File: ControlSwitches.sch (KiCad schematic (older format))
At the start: 17 parts, among them J6 Backup, SW1 HAZARD, SW2 CRUISE_SET, SW3 CRUISE, SW4 F/R_SW, SW5 HEADLIGHT_SW, SW6 BACKUP_SW, SW7 TURN_SIGNAL_SW, SW8 REGEN_SW

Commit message: Finished current updates to the board
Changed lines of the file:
@@
 Wire Wire Line
 	7950 4700 8800 4700
+Text Label 8800 4900 2    50   ~ 0
+FOR_SW
+Text Label 8800 4700 2    50   ~ 0
+REV_SW
 $EndSCHEMATC

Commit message: Changed switches
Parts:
- added R?: 10k, symbol Device:R_US
- SW1, SW5, SW6: footprint Connector_Molex:Molex_Micro-Fit_3.0_43650-0300_1x03_P3.00mm_Horizontal -> Connector_Molex:Molex_Micro-Fit_3.0_43650-0200_1x02_P3.00mm_Horizontal; symbol Switch:SW_SPDT -> Switch:SW_SPST
- SW2, SW3, SW8: footprint Connector_Molex:Molex_Micro-Fit_3.0_43650-0300_1x03_P3.00mm_Horizontal -> Connector_Molex:Molex_Micro-Fit_3.0_43650-0200_1x02_P3.00mm_Horizontal; symbol Switch:SW_SPDT -> Switch:SW_Push
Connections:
- net +3V3: no longer R5.2, R6.2, R7.2, R9.2, SW5.3 (C)
- net Backup: now also SW6.1 (A); no longer SW6.2 (B)
- net CRUZ_EN: now also SW3.1; no longer SW3.2 (B)
- net CRUZ_ST: now also SW2.1; no longer SW2.2 (B)
- net GND: now also R5.2, R6.2, R7.2, R9.2, R?.2; no longer SW1.1 (A), SW2.1 (A), SW3.1 (A), SW5.1 (A), SW8.1 (A)
- net GNDPWR: now also SW6.2 (B); no longer SW6.1 (A)
- net HZD_SW: now also SW1.1 (A); no longer SW1.2 (B)
- net Headlight_SW: now also SW5.1 (A); no longer SW5.2 (B)
- net REGEN_SW: now also SW8.1; no longer SW8.2 (B)
- net at R6.1: now also SW2.2; no longer SW2.3 (C)
- net at R7.1: now also SW3.2; no longer SW3.3 (C)
- net at R5.1: now also SW1.2 (B); no longer SW1.3 (C)
- net at R9.1: now also SW8.2; no longer SW8.3 (C)
- removed net +12V: SW6.3 (C)
- new net: R?.1, SW5.2 (B)
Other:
- moved on the sheet: J2, R13, R14, R15, R16, R17, R19, R20, R9, SW4, SW7

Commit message: Board finished with the new changes, needs to be checked
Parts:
- R21: renamed from R?; footprint (none) -> Resistor_SMD:R_0805_2012Metric
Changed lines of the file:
@@
 	3250 3200 3400 3200
 $Comp
-L power:GND #PWR?
+L power:GND #PWR011
 U 1 1 600A77A8
 P 3250 3200
-F 0 "#PWR?" H 3250 2950 50  0001 C CNN
+F 0 "#PWR011" H 3250 2950 50  0001 C CNN
 F 1 "GND" H 3255 3027 50  0000 C CNN
 F 2 "" H 3250 3200 50  0001 C CNN
@@
 $EndComp
 $Comp
-L Device:R_US R?
+L Device:R_US R21
 U 1 1 600A937F
 P 5450 4050
-F 0 "R?" V 5245 4050 50  0000 C CNN
+F 0 "R21" V 5245 4050 50  0000 C CNN
 F 1 "10k" V 5336 4050 50  0000 C CNN
-F 2 "" V 5490 4040 50  0001 C CNN
+F 2 "Resistor_SMD:R_0805_2012Metric" V 5490 4040 50  0001 C CNN
 F 3 "~" H 5450 4050 50  0001 C CNN
 	1    5450 4050

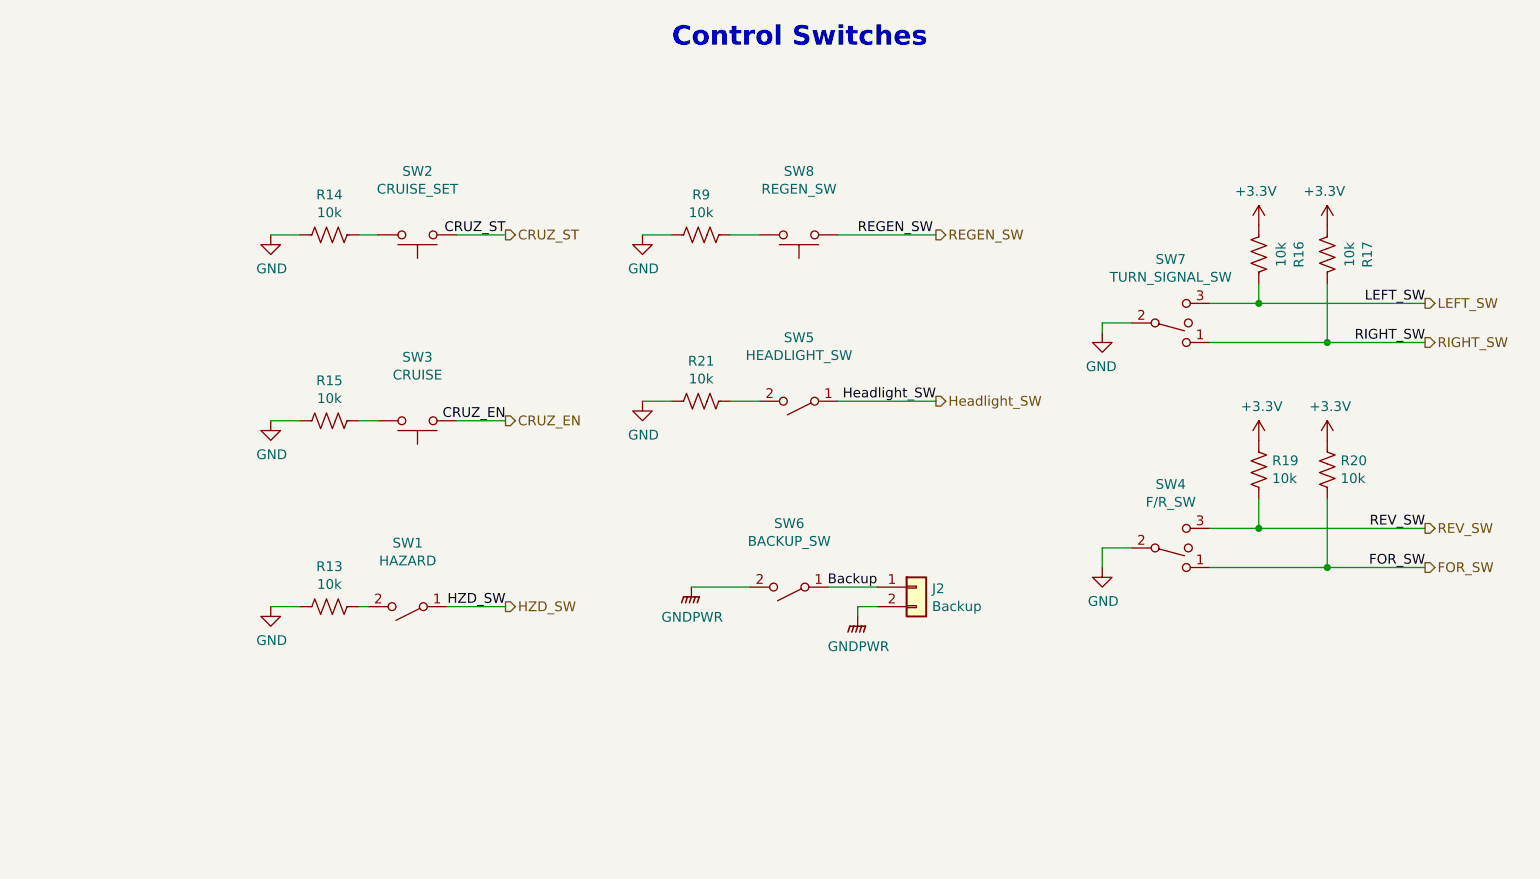
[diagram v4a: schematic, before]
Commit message: Fixes switch/button circuitry
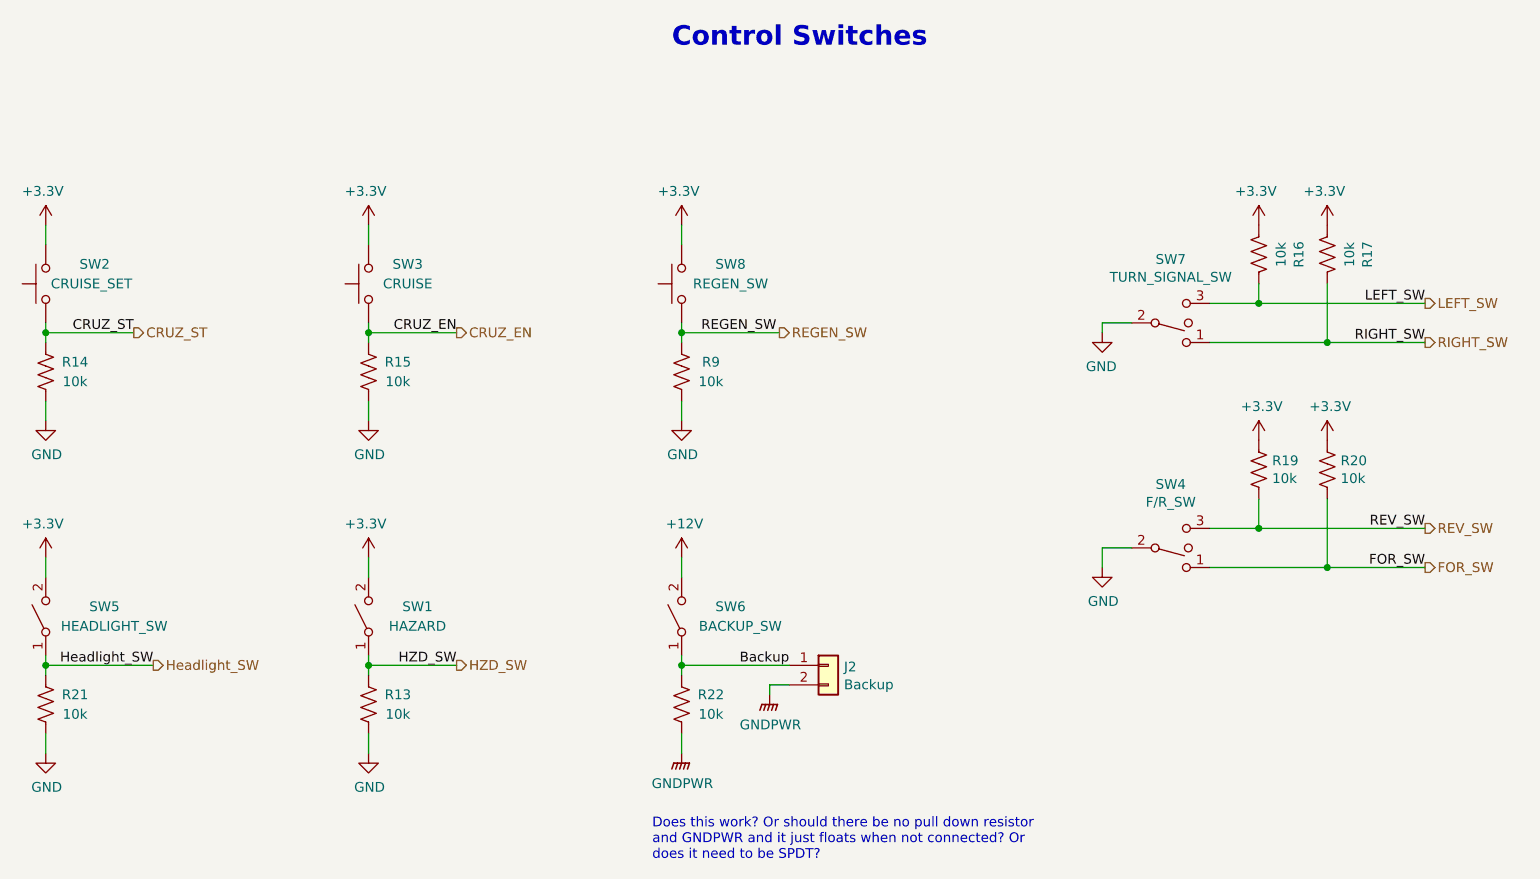
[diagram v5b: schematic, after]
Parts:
- added R22: 10k, Resistor_SMD:R_0805_2012Metric, symbol Device:R_US
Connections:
- net +3V3: now also SW1.2 (B), SW2.2, SW3.2, SW5.2 (B), SW8.2
- net Backup: now also R22.2
- net CRUZ_EN: now also R7.2
- net CRUZ_ST: now also R6.1
- net GND: now also R21.1, R5.1, R7.1, R9.1; no longer R21.2, R5.2, R7.2, R9.2
- net GNDPWR: now also R22.1; no longer SW6.2 (B)
- net HZD_SW: now also R5.2
- net Headlight_SW: now also R21.2
- net REGEN_SW: now also R9.2
- new net +12V: SW6.2 (B)
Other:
- note added: "Does this work? Or should there be no pull down resistor\nand GNDPWR and it just floats when not connected? Or \ndoes it need to be SPDT?"
- moved on the sheet: J2, R13, R14, R15, R21, R9, SW1, SW2, SW3, SW5, SW6, SW8

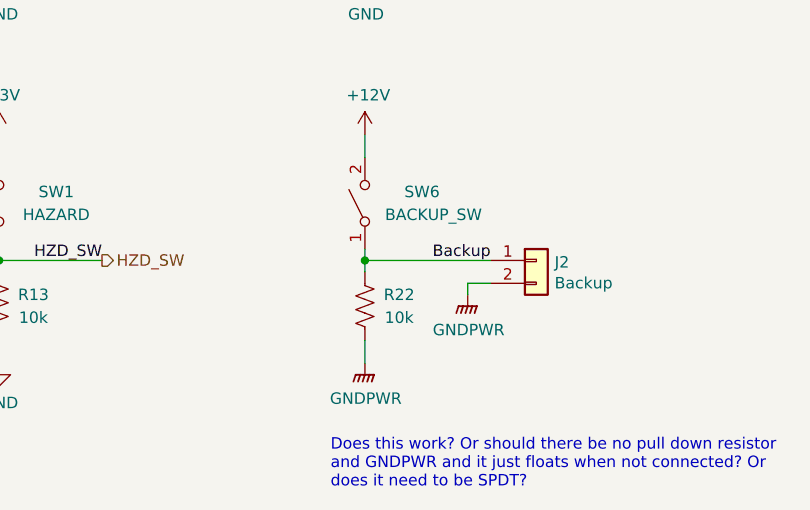
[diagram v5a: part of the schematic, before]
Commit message: isoSPI -> SPI 2
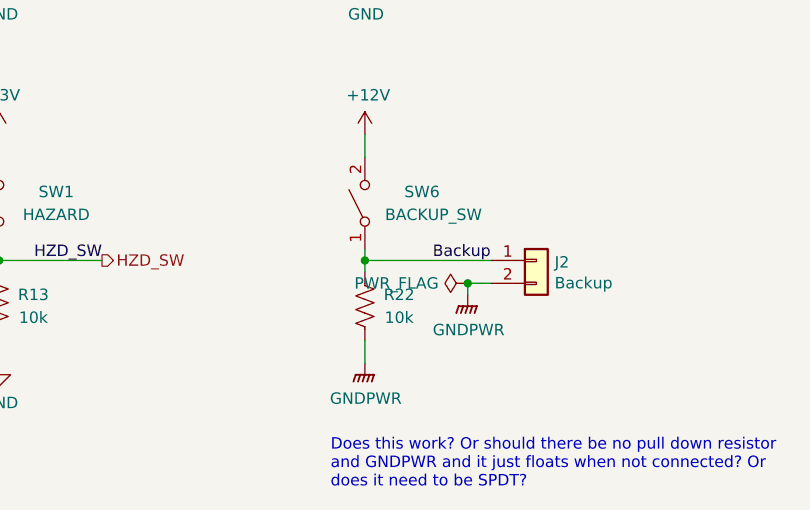
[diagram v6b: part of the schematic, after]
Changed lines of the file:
@@
 Text Notes 5200 6400 0    50   ~ 0
 Does this work? Or should there be no pull down resistor\nand GNDPWR and it just floats when not connected? Or \ndoes it need to be SPDT?
+$Comp
+L power:PWR_FLAG #FLG0102
+U 1 1 61A04CAB
+P 5800 5500
+F 0 "#FLG0102" H 5800 5575 50  0001 C CNN
+F 1 "PWR_FLAG" V 5800 5627 50  0000 L CNN
+F 2 "" H 5800 5500 50  0001 C CNN
+F 3 "~" H 5800 5500 50  0001 C CNN
+	1    5800 5500
+	0    -1   -1   0
+$EndComp
+Connection ~ 5800 5500
 $EndSCHEMATC

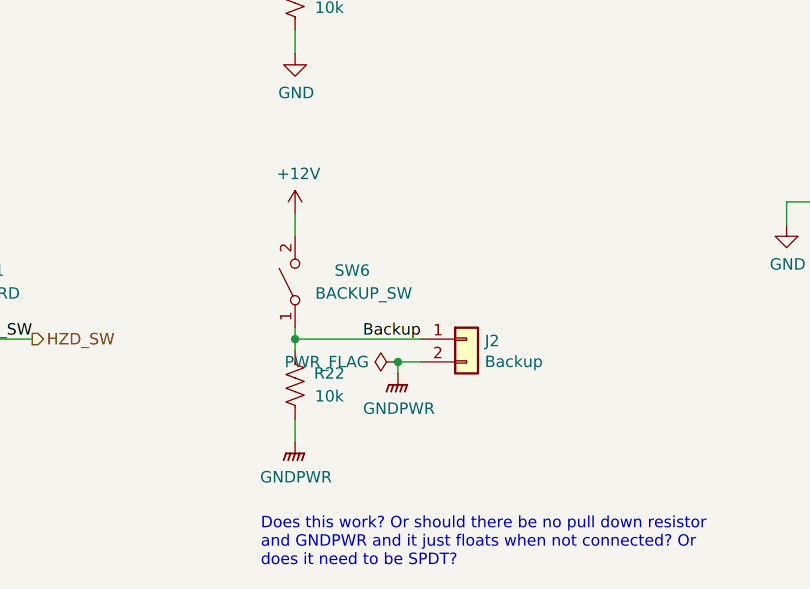
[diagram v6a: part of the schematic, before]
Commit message: Deleted backup camera
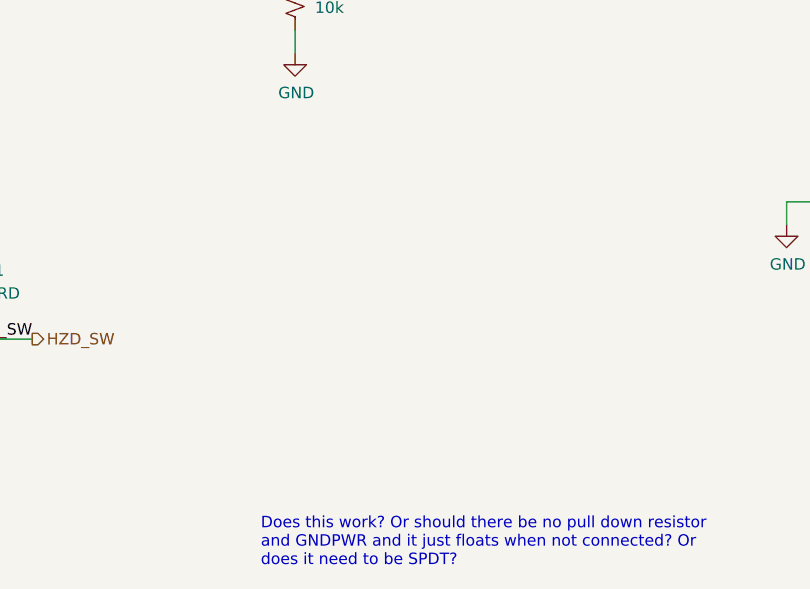
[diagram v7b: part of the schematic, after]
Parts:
- removed J6: Backup, Connector_Molex:Molex_Micro-Fit_3.0_43650-0200_1x02_P3.00mm_Horizontal, symbol Connector_Generic:Conn_01x02
- removed R22: 10k, Resistor_SMD:R_0805_2012Metric, symbol Device:R_US
- removed SW6: BACKUP_SW, Connector_Molex:Molex_Micro-Fit_3.0_43650-0200_1x02_P3.00mm_Horizontal, symbol Switch:SW_SPST
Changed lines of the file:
@@
 RIGHT_SW
-$Comp
-L Switch:SW_SPST SW?
-U 1 1 5F95FD6B
-P 5350 5150
-AR Path="/5F95FD6B" Ref="SW?"  Part="1"
-AR Path="/5F958945/5F95FD6B" Ref="SW6"  Part="1"
-AR Path="/5F78B3EB/5F95FD6B" Ref="SW6"  Part="1"
-F 0 "SW6" V 5400 4900 50  0000 C CNN
-F 1 "BACKUP_SW" V 5300 4850 50  0000 C CNN
-F 2 "Connector_Molex:Molex_Micro-Fit_3.0_43650-0200_1x02_P3.00mm_Horizontal" H 5350 5150 50  0001 C CNN
-F 3 "~" H 5350 5150 50  0001 C CNN
-	1    5350 5150
-	0    -1   -1   0
-$EndComp
-Text Label 5900 5400 2    50   ~ 0
-Backup
 $Comp
 L power:GND #PWR?
@@
 	0    -1   -1   0
 $EndComp
-$Comp
-L Connector_Generic:Conn_01x02 J?
-U 1 1 5F95FD8F
-P 6100 5400
-AR Path="/5F95FD8F" Ref="J?"  Part="1"
-AR Path="/5F958945/5F95FD8F" Ref="J6"  Part="1"
-AR Path="/5F78B3EB/5F95FD8F" Ref="J2"  Part="1"
-F 0 "J2" H 6180 5392 50  0000 L CNN
-F 1 "Backup" H 6180 5301 50  0000 L CNN
-F 2 "Connector_Molex:Molex_Micro-Fit_3.0_43650-0200_1x02_P3.00mm_Horizontal" H 6100 5400 50  0001 C CNN
-F 3 "~" H 6100 5400 50  0001 C CNN
-	1    6100 5400
-	1    0    0    -1
-$EndComp
-$Comp
-L power:GNDPWR #PWR?
-U 1 1 5F95FD95
-P 5800 5550
-AR Path="/5F95FD95" Ref="#PWR?"  Part="1"
-AR Path="/5F958945/5F95FD95" Ref="#PWR0138"  Part="1"
-AR Path="/5F78B3EB/5F95FD95" Ref="#PWR0131"  Part="1"
-F 0 "#PWR0131" H 5800 5350 50  0001 C CNN
-F 1 "GNDPWR" H 5804 5396 50  0000 C CNN
-F 2 "" H 5800 5500 50  0001 C CNN
-F 3 "" H 5800 5500 50  0001 C CNN
-	1    5800 5550
-	1    0    0    -1
-$EndComp
-Wire Wire Line
-	5800 5550 5800 5500
-Wire Wire Line
-	5800 5500 5900 5500
 $Comp
 L Device:R_US R?
@@
 Wire Wire Line
 	3750 5750 3750 5850
-$Comp
-L power:+12V #PWR026
-U 1 1 5FE1F02E
-P 5350 4850
-F 0 "#PWR026" H 5350 4700 50  0001 C CNN
-F 1 "+12V" H 5365 5023 50  0000 C CNN
-F 2 "" H 5350 4850 50  0001 C CNN
-F 3 "" H 5350 4850 50  0001 C CNN
-	1    5350 4850
-	1    0    0    -1
-$EndComp
-$Comp
-L Device:R_US R?
-U 1 1 5FE23776
-P 5350 5600
-AR Path="/5FE23776" Ref="R?"  Part="1"
-AR Path="/5F958945/5FE23776" Ref="R?"  Part="1"
-AR Path="/5F78B3EB/5FE23776" Ref="R22"  Part="1"
-F 0 "R22" H 5200 5550 50  0000 C CNN
-F 1 "10k" H 5200 5650 50  0000 C CNN
-F 2 "Resistor_SMD:R_0805_2012Metric" V 5390 5590 50  0001 C CNN
-F 3 "~" H 5350 5600 50  0001 C CNN
-F 4 "71-CRCW080510K0FKEAC " H 5350 5600 50  0001 C CNN "Mouser Part Number"
-	1    5350 5600
-	-1   0    0    1
-$EndComp
-$Comp
-L power:GNDPWR #PWR?
-U 1 1 5FE24C12
-P 5350 5850
-AR Path="/5FE24C12" Ref="#PWR?"  Part="1"
-AR Path="/5F958945/5FE24C12" Ref="#PWR?"  Part="1"
-AR Path="/5F78B3EB/5FE24C12" Ref="#PWR027"  Part="1"
-F 0 "#PWR027" H 5350 5650 50  0001 C CNN
-F 1 "GNDPWR" H 5354 5696 50  0000 C CNN
-F 2 "" H 5350 5800 50  0001 C CNN
-F 3 "" H 5350 5800 50  0001 C CNN
-	1    5350 5850
-	1    0    0    -1
-$EndComp
-Wire Wire Line
-	5350 4850 5350 4950
-Wire Wire Line
-	5350 5350 5350 5400
-Wire Wire Line
-	5350 5400 5900 5400
-Connection ~ 5350 5400
-Wire Wire Line
-	5350 5400 5350 5450
-Wire Wire Line
-	5350 5850 5350 5750
 Text Notes 5200 6400 0    50   ~ 0
 Does this work? Or should there be no pull down resistor\nand GNDPWR and it just floats when not connected? Or \ndoes it need to be SPDT?
-$Comp
-L power:PWR_FLAG #FLG0102
-U 1 1 61A04CAB
-P 5800 5500
-F 0 "#FLG0102" H 5800 5575 50  0001 C CNN
-F 1 "PWR_FLAG" V 5800 5627 50  0000 L CNN
-F 2 "" H 5800 5500 50  0001 C CNN
-F 3 "~" H 5800 5500 50  0001 C CNN
-	1    5800 5500
-	0    -1   -1   0
-$EndComp
-Connection ~ 5800 5500
 $EndSCHEMATC
